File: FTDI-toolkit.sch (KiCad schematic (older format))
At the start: 83 parts, among them IC1 TLV70033DCKT, IC12 SN74LV1T125DCKR, IC13 74HC00BQ, IC15 TS5A3359, IC2 TLV70018DCKT, IC3 TS5A3359, IC7 SN74LV1T125DCKR, IC8 FT2232D, Y1 MQ-6.000-12-30/30/

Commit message: Update sch&footprint libraries, unify LEDs, change ferrite beads
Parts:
- removed USB1: ~, FTDI-toolkit:LED0603, symbol FTDI-toolkit:LED
- added USB1: KPT-1608SGC, antmicro-footprints:LED_0603, symbol antmicroLEDIndicationDiscrete:LG_L29K-G2J1-24-Z
- 1V8_A1, 1V8_B1, 3V3_A1, 3V3_B1, 5V0_A1, 5V0_B1, RX_A1, RX_B1, TX_A1, TX_B1: footprint FTDI-toolkit:LED0603 -> antmicro-footprints:LED_0603; symbol FTDI-toolkit:LG_L29K-G2J1-24-Z- -> antmicroLEDIndicationDiscrete:LG_L29K-G2J1-24-Z; MPN KPT-1608SGC -> LG L29K-G2J1-24-Z; Manufacturer KINGBRIGHT -> OSRAM Opto Semiconductors Inc.
- C1, C2, C5, C6: footprint FTDI-toolkit:0603 -> antmicro-footprints:0603-cap; symbol FTDI-toolkit:C_1u_0603 -> antmicroCapacitors0603:C_1u_0603; MPN (none) -> 0603YD105KAT2A; Manufacturer (none) -> WALSIN; Val (none) -> 1u
- C10, C11, C12, C13, C14, C15, C16, C19, C20, C21, C22, C4, C7, C8, C9: footprint FTDI-toolkit:0402 -> antmicro-footprints:0402-cap; symbol FTDI-toolkit:C_100n_0402_16V- -> antmicroCapacitors0402:C_100n_0402_16V
- C17, C18: footprint FTDI-toolkit:0402 -> antmicro-footprints:0402-cap; symbol FTDI-toolkit:C_27p_0402- -> antmicroCapacitors0402:C_27p_0402
- C3: footprint FTDI-toolkit:0402 -> antmicro-footprints:0402-cap; symbol FTDI-toolkit:C_10n_0402 -> antmicroCapacitors0402:C_10n_0402
- D1: footprint FTDI-toolkit:SOT-3 -> antmicro-footprints:SOT-3; symbol FTDI-toolkit:TPD2E009 -> antmicroTVSDiodes:TPD2E009
- D2: footprint FTDI-toolkit:TPD6E05U06_PASS -> antmicro-footprints:TPD6E05U06; symbol FTDI-toolkit:TPD6E05U06 -> antmicroTVSDiodes:TPD6E05U06; Manufacturer (none) -> Texas Instruments
- IC1: footprint FTDI-toolkit:SC70-5 -> Package_TO_SOT_SMD:SOT-353_SC-70-5; symbol FTDI-toolkit:TLV700 -> Regulator_Linear:TLV70033_SOT353
- IC10, IC11, IC4, IC6: symbol FTDI-toolkit:SN74LV1T125 -> antmicroLogicTranslatorsLevelShifters:SN74LV1T125
- IC12, IC5, IC7, IC9: footprint FTDI-toolkit:SC70-5 -> antmicro-footprints:SC70-5; symbol FTDI-toolkit:SN74LV1T125 -> antmicroLogicTranslatorsLevelShifters:SN74LV1T125
- IC13: footprint FTDI-toolkit:DHVQFN14 -> antmicro-footprints:DHVQFN14; symbol FTDI-toolkit:74HC00BQ -> antmicroLogicGatesandInverters:74HC00BQ
- IC15, IC3: footprint FTDI-toolkit:TS5A3359 -> antmicro-footprints:TS5A3359; symbol FTDI-toolkit:TS5A3359 -> antmicroInterfaceAnalogSwitchesMultiplexersDemultiplexers:TS5A3359
- IC2: footprint FTDI-toolkit:SC70-5 -> Package_TO_SOT_SMD:SOT-353_SC-70-5; symbol FTDI-toolkit:TLV700 -> Regulator_Linear:TLV70018_SOT353
- IC8: footprint FTDI-toolkit:LQFP-48 -> antmicro-footprints:LQFP-48_7x7mm; symbol FTDI-toolkit:FT2232 -> antmicroInterfaceControllers:FT2232D
- J1: footprint FTDI-toolkit:WE_629105150521 -> antmicro-footprints:USB_Micro_B_Female_629105150521; symbol FTDI-toolkit:Micro_USB_B -> antmicroUSBDVIHDMIConnectors:WE_629105150521; MPN (none) -> 629105150521; Manufacturer (none) -> Wurth_Elektronik
- J2: footprint FTDI-toolkit:SHF-105-01-X-D-SM -> antmicro-footprints:SHF-105-01-X-D-SM; symbol FTDI-toolkit:2X05 -> antmicroRectangularConnectorsHeadersMalePins:2X05
- J3: footprint FTDI-toolkit:MH_2X08_2.54_RA -> antmicro-footprints:MH_2X08_2.54_RA; symbol FTDI-toolkit:2X08 -> antmicroRectangularConnectorsHeadersMalePins:2X08
- L1, L2: value BLM18SG121TN1D -> BLM18PG121SN1D; footprint FTDI-toolkit:0603 -> antmicro-footprints:0603-res; symbol FTDI-toolkit:Inductor_SMT -> antmicroFerriteBeadsandChips:BLM18PG121SN1D; MPN (none) -> BLM18PG121SN1D; Manufacturer (none) -> Murata Electronics North America
- N1: footprint FTDI-toolkit:antmicro-logo_scaled_12mm -> antmicro-footprints:antmicro-logo; symbol FTDI-toolkit:antmicro_logo -> antmicroMechanicalParts:antmicro_logo
- N2: footprint FTDI-toolkit:OSHW-Logo2_7.3x6mm_SilkScreen -> antmicro-footprints:oshw-logo; symbol FTDI-toolkit:oshw_logo -> antmicroMechanicalParts:oshw_logo
- R1, R11, R12, R14, R15, R18, R3, R6, R7, R8: footprint FTDI-toolkit:0402 -> antmicro-footprints:0402-res; symbol FTDI-toolkit:R_220R_0402- -> antmicroResistors0402:R_220R_0402; MPN CRG0402J220R -> ERJ2GEJ221X; Manufacturer TE_CONNECTIVITY_/_NEOHM -> Panasonic
- R10: footprint FTDI-toolkit:0402 -> antmicro-footprints:0402-res; symbol FTDI-toolkit:R_1k54_0402- -> antmicroResistors0402:R_1k54_0402
- R13, R16, R17, R19, R22, R4, R5: footprint FTDI-toolkit:0402 -> antmicro-footprints:0402-res; symbol FTDI-toolkit:R_10k_0402- -> antmicroResistors0402:R_10k_0402
- R2: footprint FTDI-toolkit:0402 -> antmicro-footprints:0402-res; symbol FTDI-toolkit:R_470R_0402 -> antmicroResistors0402:R_470R_0402; MPN CRCW0402470RFKED. -> CRCW0402470RFKED
- R20, R23, R24: footprint FTDI-toolkit:0402 -> antmicro-footprints:0402-res; symbol FTDI-toolkit:R_0R_0402- -> antmicroResistors0402:R_0R_0402
- R21: footprint FTDI-toolkit:0402 -> antmicro-footprints:0402-res; symbol FTDI-toolkit:R_4k7_0402- -> antmicroResistors0402:R_4k7_0402
- R9: footprint FTDI-toolkit:0402 -> antmicro-footprints:0402-res; symbol FTDI-toolkit:R_470R_0402- -> antmicroResistors0402:R_470R_0402; MPN CRCW0402470RFKED. -> CRCW0402470RFKED
- SW1_A1: footprint FTDI-toolkit:MH_1X03_2.54 -> antmicro-footprints:MH_1X03_2.54; symbol FTDI-toolkit:1X03 -> antmicroRectangularConnectorsHeadersMalePins:1X03
- SW1_B1: symbol FTDI-toolkit:1X03 -> antmicroRectangularConnectorsHeadersMalePins:1X03
- Y1: symbol FTDI-toolkit:CRYSTAL_6Mhz -> antmicroCrystals:CRYSTAL_6Mhz
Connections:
- wire segments 278 -> 267

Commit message: Layout updates
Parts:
- N1: footprint antmicro-footprints:antmicro-logo -> antmicro-footprints:antmicro-logo_scaled_12mm
- N2: footprint antmicro-footprints:oshw-logo -> antmicro-footprints:OSHW-Logo2_7.3x6mm_SilkScreen
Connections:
- wire segments 267 -> 290
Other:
- moved on the sheet: C18, R13
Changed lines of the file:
@@
 Wire Wire Line
 	12100 2050 12100 1800
-Wire Wire Line
-	9050 8950 8150 8950
-Wire Wire Line
-	7750 9300 7700 9300
-Text GLabel 8750 9350 0    50   Input ~ 0
+Text GLabel 8650 9350 0    50   Input ~ 0
 5V_USB
 Wire Wire Line
@@
 	3950 10100 4150 10100
 Wire Wire Line
-	7750 8850 9050 8850
+	7700 8850 9050 8850
 Text GLabel 5250 10400 1    50   Input ~ 0
 VCCIOB
@@
 Review connections!!!!
 Wire Wire Line
-	6450 5800 6950 5800
-Wire Wire Line
 	8750 1850 8750 1950
 Wire Wire Line
@@
 Wire Wire Line
 	1500 1500 1850 1500
-Wire Wire Line
-	8150 8950 8150 9300
-Wire Wire Line
-	7750 8850 7750 9300
-Wire Wire Line
-	6450 4900 6450 5800
-Wire Wire Line
-	9050 9550 9050 10450
 Wire Wire Line
 	4250 1550 4250 1500
@@
 F 0 "N2" H 11244 10853 50  0000 L CNN
 F 1 "oshw_logo" H 11244 10762 50  0000 L CNN
-F 2 "antmicro-footprints:oshw-logo" H 11070 10610 50  0001 C CNN
+F 2 "antmicro-footprints:OSHW-Logo2_7.3x6mm_SilkScreen" H 11070 10610 50  0001 C CNN
 F 3 "" H 11050 10850 50  0001 C CNN
 	1    11050 10850
@@
 F 0 "N1" H 10314 11043 50  0000 L CNN
 F 1 "antmicro_logo" H 10314 10952 50  0000 L CNN
-F 2 "antmicro-footprints:antmicro-logo" H 10000 11200 50  0001 C CNN
+F 2 "antmicro-footprints:antmicro-logo_scaled_12mm" H 10000 11200 50  0001 C CNN
 F 3 "" H 10100 11300 50  0001 C CNN
 	1    10100 10950
@@
 L antmicroResistors0402:R_10k_0402 R13
 U 1 1 5F464B54
-P 8900 9350
-F 0 "R13" H 8900 9137 60  0000 C CNN
-F 1 "R_10k_0402" H 8900 9200 60  0001 C CNN
-F 2 "antmicro-footprints:0402-res" H 9100 9550 60  0001 L CNN
-F 3 "" H 8900 9350 50  0001 C CNN
-F 4 "VISHAY" H 9100 9750 60  0001 L CNN "Manufacturer"
-F 5 "CRCW040210K0FKEDHP" H 9100 9650 60  0001 L CNN "MPN"
-F 6 "10k" H 8900 9050 50  0000 C CNN "Val"
-	1    8900 9350
+P 8850 9350
+F 0 "R13" H 8850 9137 60  0000 C CNN
+F 1 "R_10k_0402" H 8850 9200 60  0001 C CNN
+F 2 "antmicro-footprints:0402-res" H 9050 9550 60  0001 L CNN
+F 3 "" H 8850 9350 50  0001 C CNN
+F 4 "VISHAY" H 9050 9750 60  0001 L CNN "Manufacturer"
+F 5 "CRCW040210K0FKEDHP" H 9050 9650 60  0001 L CNN "MPN"
+F 6 "10k" H 8850 9050 50  0000 C CNN "Val"
+	1    8850 9350
 	1    0    0    -1
 $EndComp
@@
 L power:GND #PWR0123
 U 1 1 5FBF14DD
-P 9050 10450
-F 0 "#PWR0123" H 9050 10200 50  0001 C CNN
-F 1 "GND" H 9055 10277 50  0000 C CNN
-F 2 "" H 9050 10450 50  0001 C CNN
-F 3 "" H 9050 10450 50  0001 C CNN
-	1    9050 10450
+P 9000 10450
+F 0 "#PWR0123" H 9000 10200 50  0001 C CNN
+F 1 "GND" H 9005 10277 50  0000 C CNN
+F 2 "" H 9000 10450 50  0001 C CNN
+F 3 "" H 9000 10450 50  0001 C CNN
+	1    9000 10450
 	1    0    0    -1
 $EndComp
@@
 L power:GND #PWR0120
 U 1 1 5FB95D7E
-P 8150 9600
-F 0 "#PWR0120" H 8150 9350 50  0001 C CNN
-F 1 "GND" H 8155 9427 50  0000 C CNN
-F 2 "" H 8150 9600 50  0001 C CNN
-F 3 "" H 8150 9600 50  0001 C CNN
-	1    8150 9600
+P 8200 9600
+F 0 "#PWR0120" H 8200 9350 50  0001 C CNN
+F 1 "GND" H 8205 9427 50  0000 C CNN
+F 2 "" H 8200 9600 50  0001 C CNN
+F 3 "" H 8200 9600 50  0001 C CNN
+	1    8200 9600
 	1    0    0    -1
 $EndComp
@@
 L antmicroCapacitors0402:C_27p_0402 C18
 U 1 1 5F401E5E
-P 8150 9450
-F 0 "C18" H 8265 9495 60  0000 L CNN
-F 1 "C_27p_0402" H 8150 9300 60  0001 C CNN
-F 2 "antmicro-footprints:0402-cap" H 8350 9650 60  0001 L CNN
-F 3 "" H 8150 9450 50  0001 C CNN
-F 4 "WALSIN" H 8350 9850 60  0001 L CNN "Manufacturer"
-F 5 "0402N270J500CT" H 8350 9750 60  0001 L CNN "MPN"
-F 6 "27p" H 8300 9600 50  0000 L CNN "Val"
-	1    8150 9450
+P 8200 9450
+F 0 "C18" H 8315 9495 60  0000 L CNN
+F 1 "C_27p_0402" H 8200 9300 60  0001 C CNN
+F 2 "antmicro-footprints:0402-cap" H 8400 9650 60  0001 L CNN
+F 3 "" H 8200 9450 50  0001 C CNN
+F 4 "WALSIN" H 8400 9850 60  0001 L CNN "Manufacturer"
+F 5 "0402N270J500CT" H 8400 9750 60  0001 L CNN "MPN"
+F 6 "27p" H 8350 9600 50  0000 L CNN "Val"
+	1    8200 9450
 	-1   0    0    1
 $EndComp
@@
 U 1 1 5E5F7C20
 P 1200 1700
-F 0 "J1" H 1450 1300 60  0000 R BNN
+F 0 "J1" H 1500 1150 60  0000 R BNN
 F 1 "~" H 1200 1700 50  0001 C CNN
 F 2 "antmicro-footprints:USB_Micro_B_Female_629105150521" H 1200 1700 50  0001 C CNN
@@
 	0    1    1    0
 $EndComp
+Wire Wire Line
+	9000 9350 9050 9350
+Wire Wire Line
+	8700 9350 8650 9350
+Wire Wire Line
+	9050 9550 9000 9550
+Wire Wire Line
+	9000 9550 9000 9850
+Wire Wire Line
+	9050 10250 9000 10250
+Connection ~ 9000 10250
+Wire Wire Line
+	9000 10250 9000 10450
+Wire Wire Line
+	9050 10150 9000 10150
+Connection ~ 9000 10150
+Wire Wire Line
+	9000 10150 9000 10250
+Wire Wire Line
+	9050 10050 9000 10050
+Connection ~ 9000 10050
+Wire Wire Line
+	9000 10050 9000 10150
+Wire Wire Line
+	9050 9950 9000 9950
+Connection ~ 9000 9950
+Wire Wire Line
+	9000 9950 9000 10050
+Wire Wire Line
+	9050 9850 9000 9850
+Connection ~ 9000 9850
+Wire Wire Line
+	9000 9850 9000 9950
+Wire Wire Line
+	7700 8850 7700 9150
+Wire Wire Line
+	8200 8950 9050 8950
+Wire Wire Line
+	8200 8950 8200 9150
+Wire Wire Line
+	8150 9150 8200 9150
+Connection ~ 8200 9150
+Wire Wire Line
+	8200 9150 8200 9300
+Wire Wire Line
+	7750 9150 7700 9150
+Connection ~ 7700 9150
+Wire Wire Line
+	7700 9150 7700 9300
+Wire Wire Line
+	6450 4900 6350 4900
+Wire Wire Line
+	6350 4900 6350 5000
+Wire Wire Line
+	6350 5800 6950 5800
+Wire Wire Line
+	6450 5000 6350 5000
+Connection ~ 6350 5000
+Wire Wire Line
+	6350 5000 6350 5200
+Wire Wire Line
+	6450 5200 6350 5200
+Connection ~ 6350 5200
+Wire Wire Line
+	6350 5200 6350 5300
+Wire Wire Line
+	6450 5300 6350 5300
+Connection ~ 6350 5300
+Wire Wire Line
+	6350 5300 6350 5800
 $EndSCHEMATC

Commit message: Start revision 1.1.0
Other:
- note added: "1.1.0 07.2020"
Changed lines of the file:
@@
 Wire Wire Line
 	6350 5300 6350 5800
+Text Notes 15450 11050 0    47   ~ 0
+1.1.0 07.2020
 $EndSCHEMATC

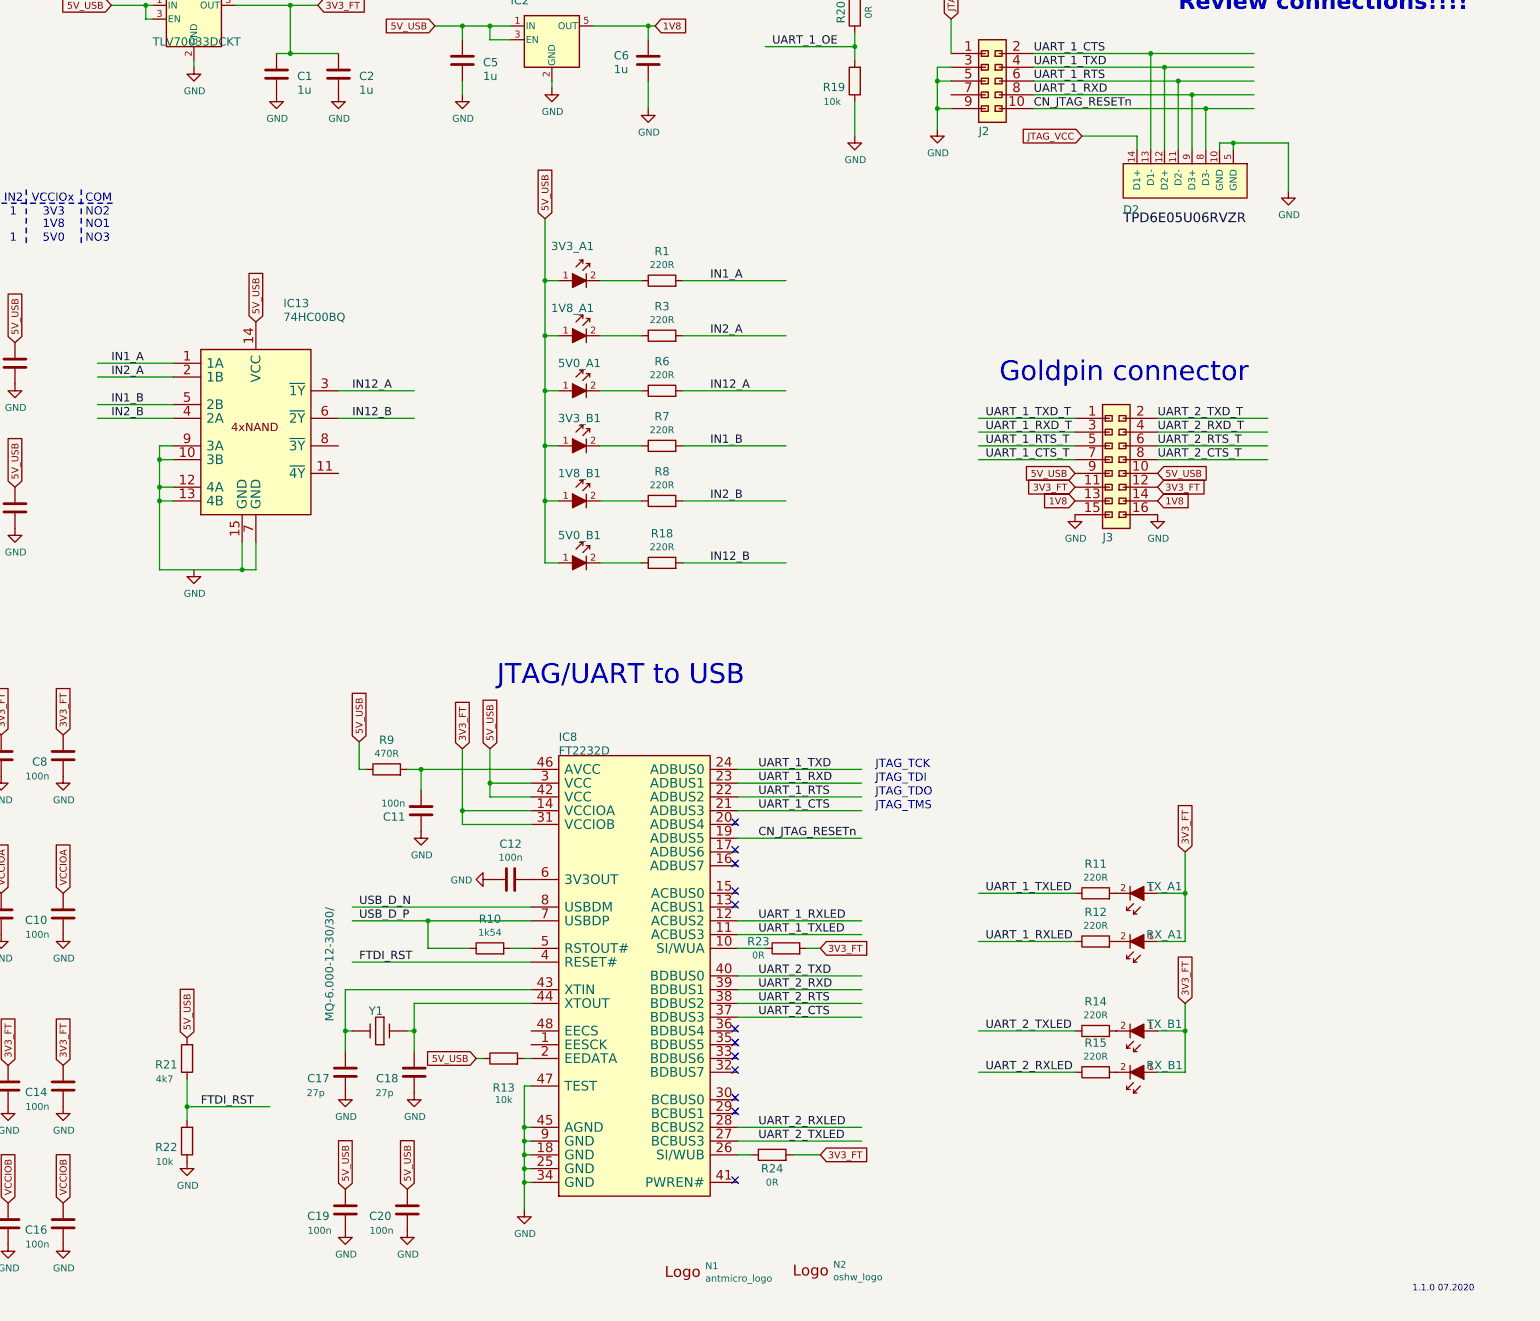
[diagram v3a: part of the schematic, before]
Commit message: Place and route FTDI2232H
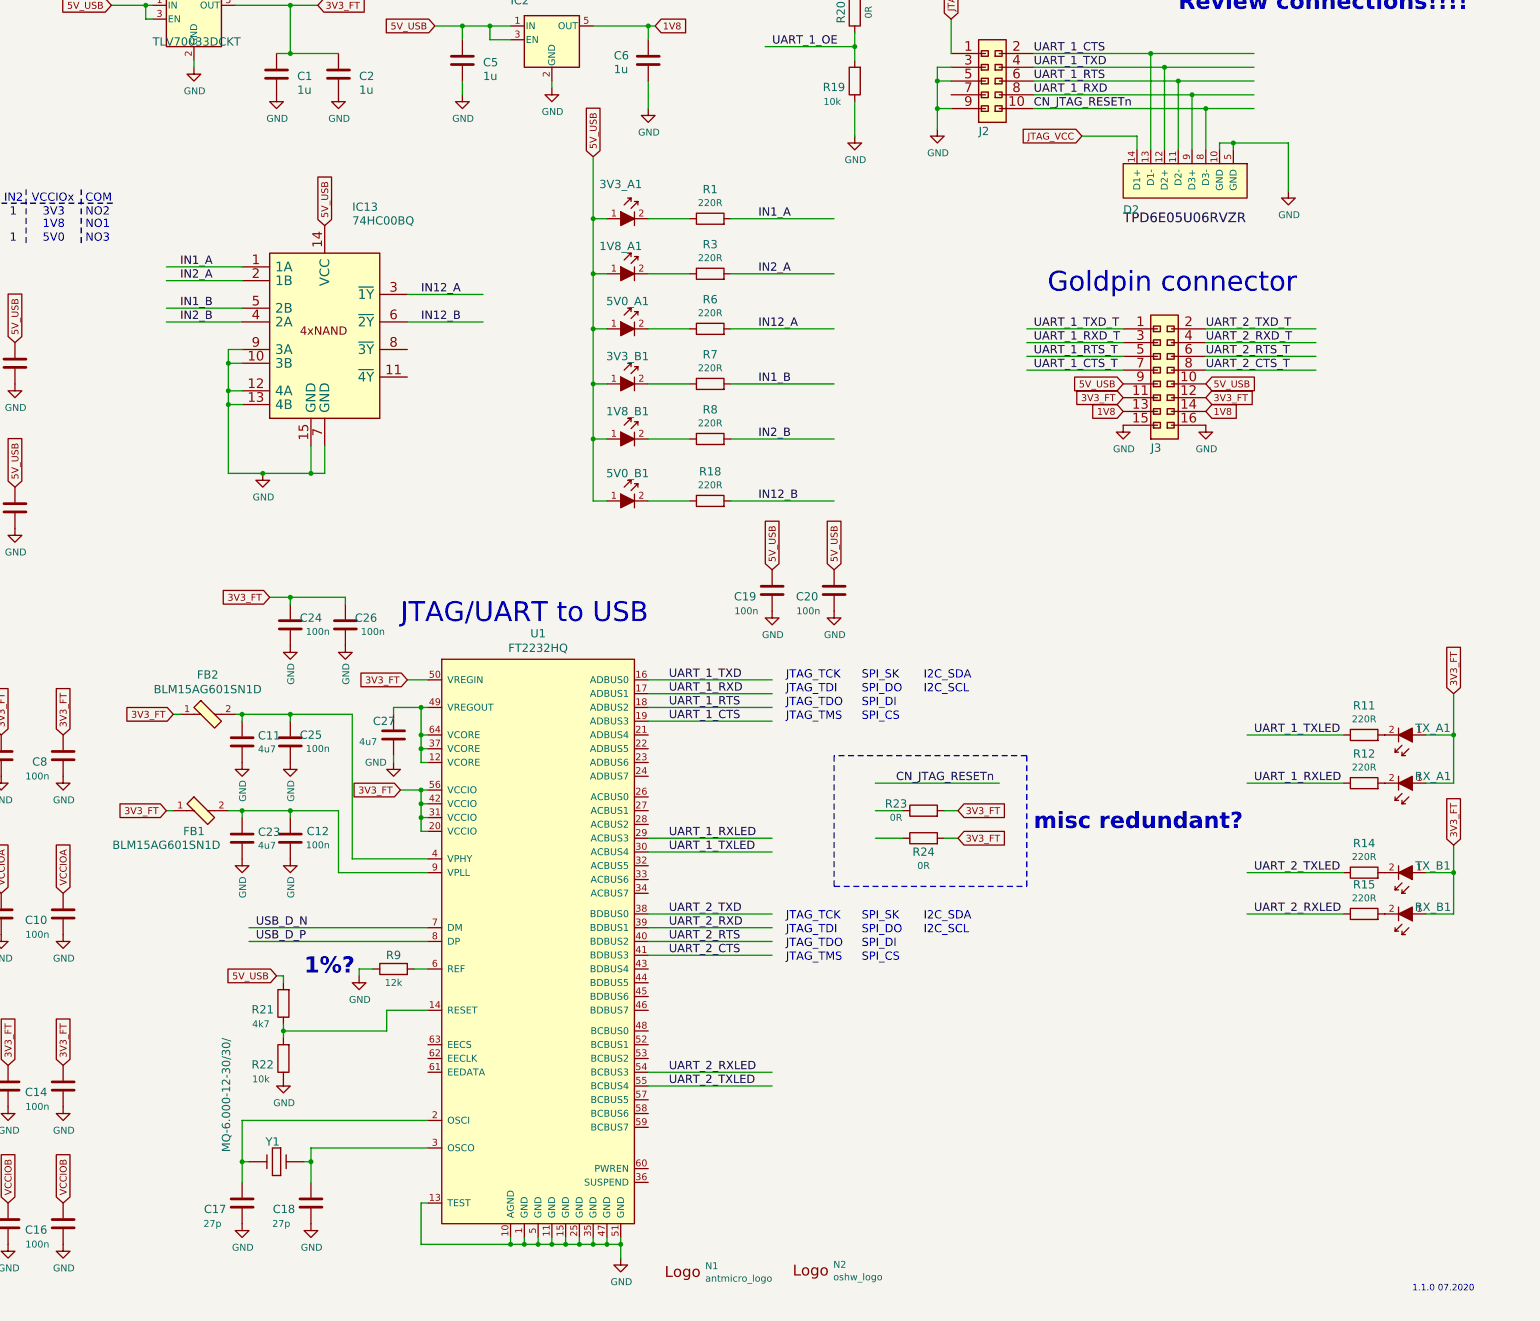
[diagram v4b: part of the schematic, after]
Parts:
- removed C11: C_100n_0402_16V, antmicro-footprints:0402-cap, symbol antmicroCapacitors0402:C_100n_0402_16V
- removed IC8: FT2232D, antmicro-footprints:LQFP-48_7x7mm, symbol antmicroInterfaceControllers:FT2232D
- removed R10: R_1k54_0402, antmicro-footprints:0402-res, symbol antmicroResistors0402:R_1k54_0402
- removed R13: R_10k_0402, antmicro-footprints:0402-res, symbol antmicroResistors0402:R_10k_0402
- removed R9: R_470R_0402, antmicro-footprints:0402-res, symbol antmicroResistors0402:R_470R_0402
- added C11, C23, C27: C_4u7_0402, antmicro-footprints:0402-cap, symbol antmicroCapacitors0402:C_4u7_0402
- added C24, C25, C26: C_100n_0402_16V, antmicro-footprints:0402-cap, symbol antmicroCapacitors0402:C_100n_0402_16V
- added FB1, FB2: BLM15AG601SN1D, antmicro-footprints:0402-res, symbol antmicroFerriteBeadsandChips:BLM15AG601SN1D
- added R9: R_12k_0402, antmicro-footprints:0402-res, symbol antmicroResistors0402:R_12k_0402
- added U1: FT2232HQ, antmicro-footprints:LQFP-64_10x10mm, symbol antmicroInterfaceControllers:FT2232HQ
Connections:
- net labels removed: FTDI_RST
- wire segments 290 -> 326
- no-connect marks 12 -> 0
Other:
- note added: "1%?\n"
- note added: "I2C_SCL"
- note added: "I2C_SDA"
- note added: "SPI_CS\n"
- note added: "SPI_DI\n"
- note added: "SPI_DO"
- note added: "SPI_SK\n"
- note added: "misc redundant?\n"
- moved on the sheet: 1V8_A1, 1V8_B1, 3V3_A1, 3V3_B1, 5V0_A1, 5V0_B1, C12, C17, C18, C19, C20, IC13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
